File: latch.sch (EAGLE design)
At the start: 32 parts, among them IC1 LM7805, IC2 LM339D, IC3 LM339D, K1 4052, Q1 BS170, Q2 BS170, Q3 BS170, Q4 BS170, Q5 BS170, Q6 BS170, Q7 BS170

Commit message: Second version of latches board
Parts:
- D3: value (none) -> 1N4148
- F1: value 500mA -> 1A
- R10, R5: value 10K -> 2.2K
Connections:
- removed net BMS_RESET_2: IMD_BMS_LATCH-3.S
- new net N$14: Q6.S, Q7.D
- net BMS_STATUS: now also IMD_BMS_LATCH-3.S
- net GND: no longer Q6.S
- net N$13: no longer Q7.D
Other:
- note added: "Drawn by: Luis Suarez"
- note added: "IMD and BMS Latching Board"
- note added: "Reviewed by:"
- note added: "Signal Value Status IMD_FAIL 1 Ok 0 Fail BMS_FAIL 1 Ok 0 Fail"
- note added: "TUC Racing 2016 Formula Student Italy"
- moved on the sheet: D3, K1, Q7

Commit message: Third version of latches board
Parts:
- removed Q1: BS170, transistor-small-signal:BS170
- removed R4: 100K, rcl:R-EU_R1206
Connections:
- removed net IMD_BMS_RESET_1: IMD_BMS_LATCH-4.S, R4.2, RESET_SWITCH.S
- removed net N$4: Q1.G, R4.1
- net DELAY_PWR: now also IMD_BMS_LATCH-4.S, RESET_SWITCH.S; no longer Q1.D
- net GND: no longer Q1.S
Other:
- moved on the sheet: IMD_BMS_LATCH-7, IMD_BMS_LATCH-8, RESET_SWITCH
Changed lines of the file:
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@@
 </layers>
 <schematic xreflabel="%F%N/%S.%C%R" xrefpart="/%S.%C%R">
+<description>IMD and BMS latching board.</description>
 <attributes>
 </attributes>
@@
 <part name="R3" library="rcl" deviceset="R-EU_" device="R1206" value="1K"/>
 <part name="P+5" library="supply1" deviceset="+5V" device=""/>
-<part name="Q1" library="transistor-small-signal" deviceset="BS170" device=""/>
-<part name="GND5" library="supply1" deviceset="GND" device=""/>
-<part name="R4" library="rcl" deviceset="R-EU_" device="R1206" value="100K"/>
 <part name="RESET_SWITCH" library="adafruit" deviceset="SPST" device=""/>
 <part name="GND6" library="supply1" deviceset="GND" device=""/>
@@
 </instance>
 <instance part="F1" gate="G$1" x="40.64" y="154.94"/>
-<instance part="IMD_BMS_LATCH" gate="-7" x="220.98" y="154.94"/>
-<instance part="IMD_BMS_LATCH" gate="-8" x="220.98" y="160.02"/>
+<instance part="IMD_BMS_LATCH" gate="-7" x="220.98" y="160.02"/>
+<instance part="IMD_BMS_LATCH" gate="-8" x="220.98" y="154.94"/>
 <instance part="IMD_BMS_LATCH" gate="-9" x="220.98" y="149.86"/>
 <instance part="IMD_BMS_LATCH" gate="-10" x="220.98" y="144.78"/>
@@
 <attribute name="VALUE" x="53.34" y="106.68" size="1.778" layer="96"/>
 </instance>
-<instance part="Q1" gate="1" x="63.5" y="58.42"/>
-<instance part="GND5" gate="1" x="66.04" y="45.72"/>
-<instance part="R4" gate="G$1" x="50.8" y="58.42" smashed="yes" rot="R180">
-<attribute name="NAME" x="49.53" y="59.9186" size="1.778" layer="95"/>
-<attribute name="VALUE" x="49.53" y="55.118" size="1.778" layer="96"/>
-</instance>
-<instance part="RESET_SWITCH" gate="G$1" x="40.64" y="48.26" smashed="yes">
-<attribute name="NAME" x="34.925" y="48.895" size="1.778" layer="95" rot="R180"/>
-<attribute name="VALUE" x="38.735" y="38.735" size="1.778" layer="96" rot="R90"/>
-</instance>
-<instance part="GND6" gate="1" x="43.18" y="27.94"/>
+<instance part="RESET_SWITCH" gate="G$1" x="60.96" y="60.96" smashed="yes">
+<attribute name="NAME" x="55.245" y="61.595" size="1.778" layer="95" rot="R180"/>
+<attribute name="VALUE" x="59.055" y="51.435" size="1.778" layer="96" rot="R90"/>
+</instance>
+<instance part="GND6" gate="1" x="63.5" y="40.64"/>
 <instance part="R7" gate="G$1" x="119.38" y="106.68" smashed="yes">
 <attribute name="NAME" x="123.19" y="110.871" size="1.778" layer="95" rot="R180"/>
@@
 <pinref part="RESET_SWITCH" gate="G$1" pin="P"/>
 <pinref part="GND6" gate="1" pin="GND"/>
-<wire x1="43.18" y1="43.18" x2="43.18" y2="35.56" width="0.1524" layer="91"/>
-<wire x1="43.18" y1="35.56" x2="43.18" y2="30.48" width="0.1524" layer="91"/>
-<wire x1="43.18" y1="35.56" x2="38.1" y2="35.56" width="0.1524" layer="91"/>
-<label x="38.1" y="35.56" size="1.778" layer="95" rot="R180" xref="yes"/>
-<junction x="43.18" y="35.56"/>
-</segment>
-</net>
-<net name="IMD_BMS_RESET_1" class="0">
-<segment>
-<pinref part="IMD_BMS_LATCH" gate="-4" pin="S"/>
-<wire x1="55.88" y1="142.24" x2="33.02" y2="142.24" width="0.1524" layer="91"/>
-<label x="55.88" y="142.24" size="1.778" layer="95" xref="yes"/>
-</segment>
-<segment>
-<pinref part="R4" gate="G$1" pin="2"/>
-<wire x1="45.72" y1="58.42" x2="43.18" y2="58.42" width="0.1524" layer="91"/>
-<wire x1="43.18" y1="58.42" x2="43.18" y2="55.88" width="0.1524" layer="91"/>
-<pinref part="RESET_SWITCH" gate="G$1" pin="S"/>
-<wire x1="43.18" y1="53.34" x2="43.18" y2="55.88" width="0.1524" layer="91"/>
-<junction x="43.18" y="55.88"/>
-<wire x1="43.18" y1="55.88" x2="38.1" y2="55.88" width="0.1524" layer="91"/>
-<label x="38.1" y="55.88" size="1.778" layer="95" rot="R180" xref="yes"/>
+<wire x1="63.5" y1="55.88" x2="63.5" y2="48.26" width="0.1524" layer="91"/>
+<wire x1="63.5" y1="48.26" x2="63.5" y2="43.18" width="0.1524" layer="91"/>
+<wire x1="63.5" y1="48.26" x2="58.42" y2="48.26" width="0.1524" layer="91"/>
+<label x="58.42" y="48.26" size="1.778" layer="95" rot="R180" xref="yes"/>
+<junction x="63.5" y="48.26"/>
 </segment>
 </net>
@@
 </segment>
 <segment>
-<pinref part="Q1" gate="1" pin="S"/>
-<pinref part="GND5" gate="1" pin="GND"/>
-<wire x1="66.04" y1="53.34" x2="66.04" y2="48.26" width="0.1524" layer="91"/>
-</segment>
-<segment>
 <pinref part="Q2" gate="1" pin="S"/>
 <pinref part="GND7" gate="1" pin="GND"/>
@@
 <segment>
 <pinref part="IMD_BMS_LATCH" gate="-8" pin="S"/>
-<wire x1="218.44" y1="160.02" x2="213.36" y2="160.02" width="0.1524" layer="91"/>
-<label x="213.36" y="160.02" size="1.778" layer="95" rot="R180" xref="yes"/>
+<wire x1="218.44" y1="154.94" x2="213.36" y2="154.94" width="0.1524" layer="91"/>
+<label x="213.36" y="154.94" size="1.778" layer="95" rot="R180" xref="yes"/>
 </segment>
 <segment>
@@
 <segment>
 <pinref part="IMD_BMS_LATCH" gate="-7" pin="S"/>
-<wire x1="218.44" y1="154.94" x2="213.36" y2="154.94" width="0.1524" layer="91"/>
-<label x="213.36" y="154.94" size="1.778" layer="95" rot="R180" xref="yes"/>
+<wire x1="218.44" y1="160.02" x2="213.36" y2="160.02" width="0.1524" layer="91"/>
+<label x="213.36" y="160.02" size="1.778" layer="95" rot="R180" xref="yes"/>
 </segment>
 <segment>
@@
 <wire x1="55.88" y1="91.44" x2="55.88" y2="86.36" width="0.1524" layer="91"/>
 <wire x1="55.88" y1="86.36" x2="50.8" y2="86.36" width="0.1524" layer="91"/>
-<pinref part="Q1" gate="1" pin="D"/>
-<wire x1="55.88" y1="86.36" x2="66.04" y2="86.36" width="0.1524" layer="91"/>
-<wire x1="66.04" y1="86.36" x2="66.04" y2="63.5" width="0.1524" layer="91"/>
-<wire x1="66.04" y1="86.36" x2="71.12" y2="86.36" width="0.1524" layer="91"/>
-<junction x="66.04" y="86.36"/>
+<wire x1="55.88" y1="86.36" x2="63.5" y2="86.36" width="0.1524" layer="91"/>
 <junction x="55.88" y="86.36"/>
 <label x="71.12" y="86.36" size="1.778" layer="95" xref="yes"/>
+<wire x1="63.5" y1="86.36" x2="71.12" y2="86.36" width="0.1524" layer="91"/>
+<wire x1="63.5" y1="86.36" x2="63.5" y2="66.04" width="0.1524" layer="91"/>
+<pinref part="RESET_SWITCH" gate="G$1" pin="S"/>
+<junction x="63.5" y="86.36"/>
 </segment>
 <segment>
@@
 <wire x1="132.08" y1="48.26" x2="132.08" y2="50.8" width="0.1524" layer="91"/>
 <label x="132.08" y="50.8" size="1.778" layer="95" rot="R90" xref="yes"/>
+</segment>
+<segment>
+<pinref part="IMD_BMS_LATCH" gate="-4" pin="S"/>
+<wire x1="55.88" y1="142.24" x2="33.02" y2="142.24" width="0.1524" layer="91"/>
+<label x="55.88" y="142.24" size="1.778" layer="95" xref="yes"/>
 </segment>
 </net>
@@
 </segment>
 </net>
-<net name="N$4" class="0">
-<segment>
-<pinref part="R4" gate="G$1" pin="1"/>
-<pinref part="Q1" gate="1" pin="G"/>
-<wire x1="55.88" y1="58.42" x2="58.42" y2="58.42" width="0.1524" layer="91"/>
-</segment>
-</net>

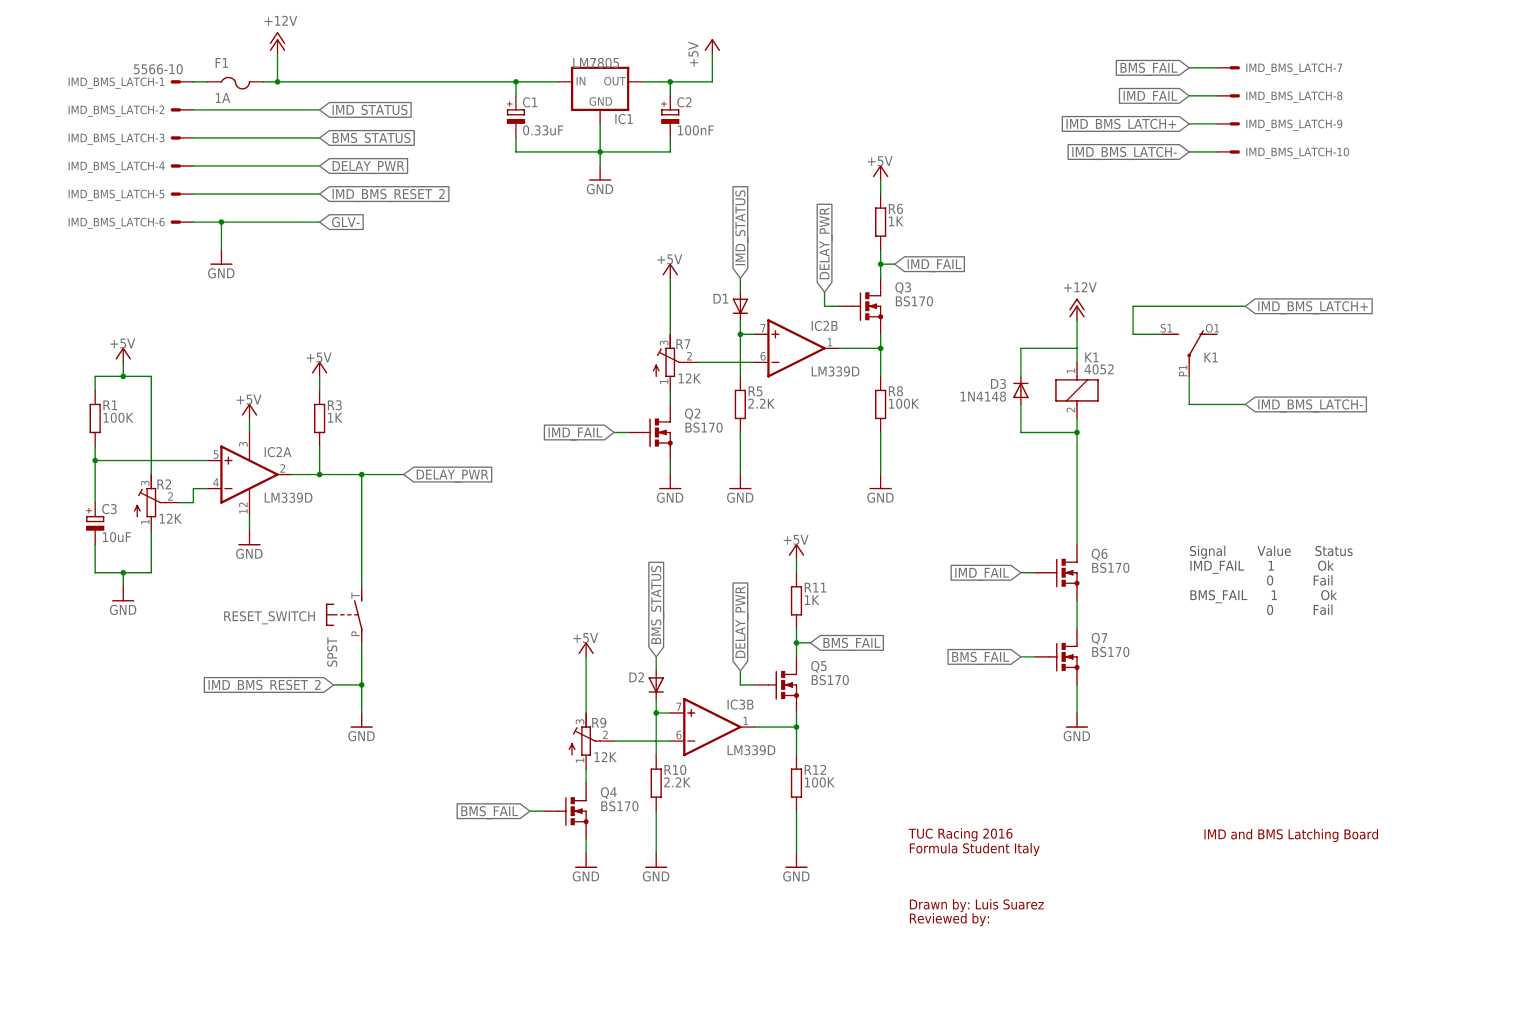
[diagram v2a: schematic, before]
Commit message: Add board design for fourth version
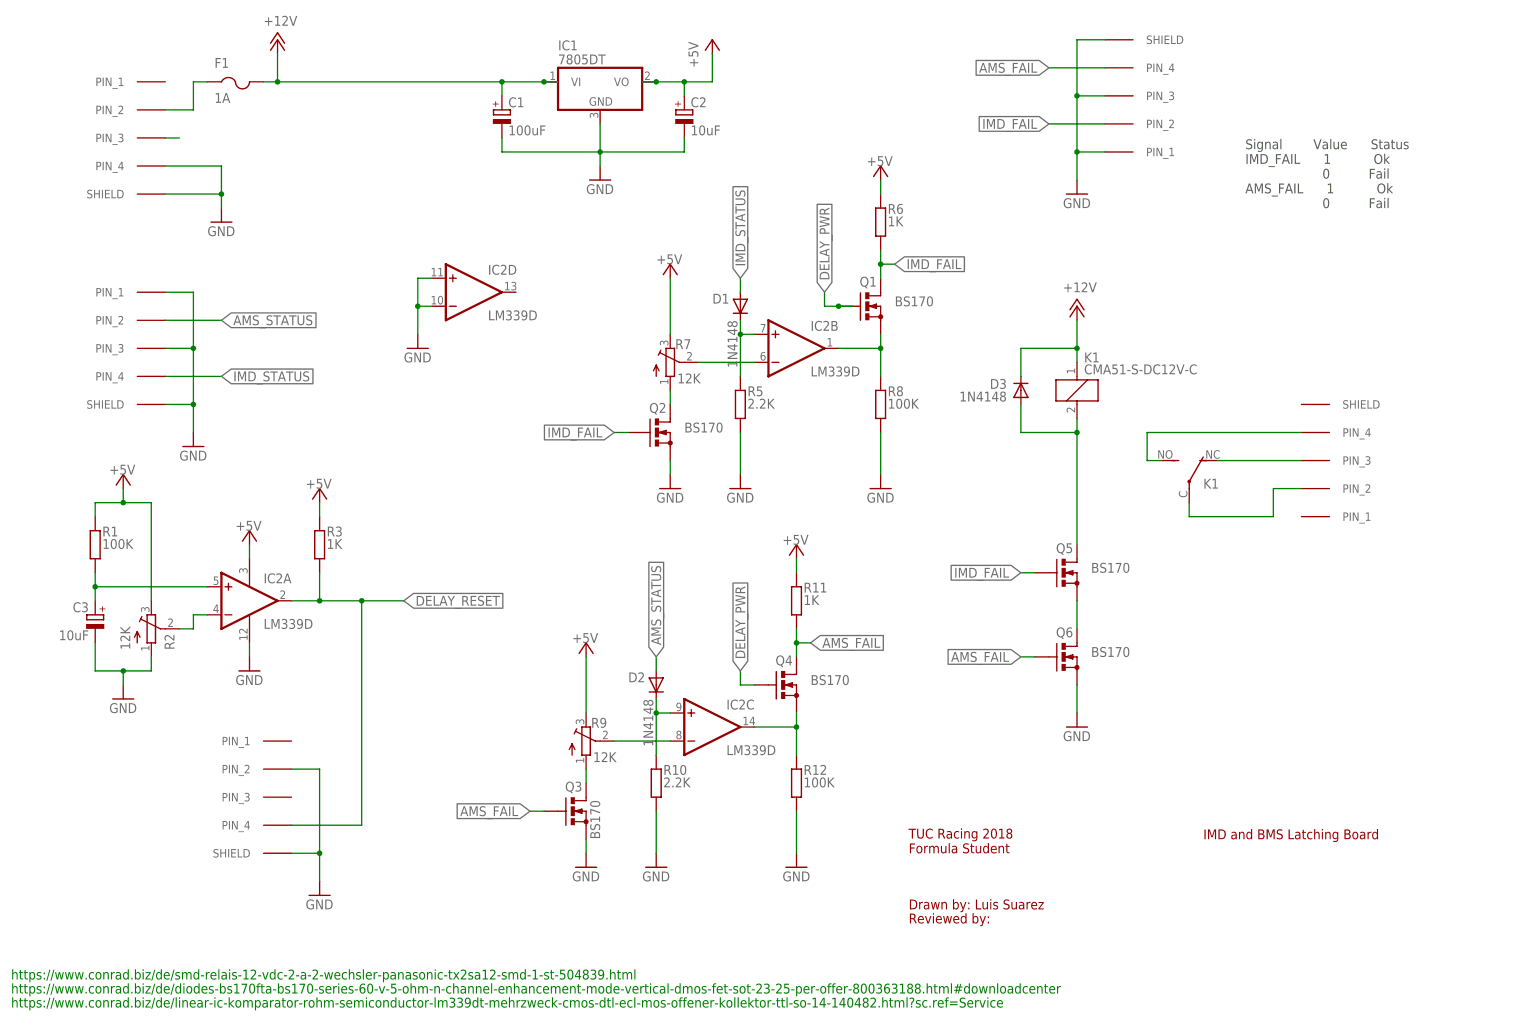
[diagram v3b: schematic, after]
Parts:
- removed IC3: LM339D, linear:LM339D
- removed IMD_BMS_LATCH: 5566-10, con-molex:5566-10
- removed Q7: BS170, transistor-small-signal:BS170
- removed RESET_SWITCH: SPST, adafruit:SPST
- added INDICATORS, RESET: M8-718-FEMALE, SamacSys_Parts:M8-718-FEMALE
- added LATCH, STATUS: M8-718-MALE, SamacSys_Parts:M8-718-MALE
- added POWER_CONN: POWER, SamacSys_Parts:M8-718-MALE
- added Q1: BS170, SamacSys_Parts:BS170FTA
- C1: value 0.33uF -> 100uF; device rcl:CPOL-EU140CLH-1010 -> rcl:CPOL-EUD
- C2: value 100nF -> 10uF; device rcl:CPOL-EU140CLH-1010 -> rcl:CPOL-EUC
- C3: device rcl:CPOL-EU140CLH-0810 -> rcl:CPOL-EUC
- D1, D2: value (none) -> 1N4148; device diode:DIODE-DO-214AC -> diode:DIODE-GF1
- F1: device adafruit:PTCFUSE-1812 -> adafruit:PTCFUSE-1206
- IC1: value LM7805 -> 7805DT; device v-reg:78XX-TO3 -> linear:7805DT
- K1: value 4052 -> CMA51-S-DC12V-C; device relay:4052 -> relay:CQ1-12V
- Q2, Q3, Q4, Q5, Q6: device transistor-small-signal:BS170 -> SamacSys_Parts:BS170FTA
- R1, R10, R11, R12, R3, R5, R6, R8: device rcl:R-EU_R1206 -> rcl:R-EU_R0805
- R2, R7, R9: device rcl:R-TRIMM64Y -> pot:TRIM_EU-SM-42/43B
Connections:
- removed net BMS_FAIL: IMD_BMS_LATCH-7.S, Q4.G, Q5.D, Q7.G, R11.1
- removed net BMS_STATUS: D2.A, IMD_BMS_LATCH-3.S
- removed net GLV-: IMD_BMS_LATCH-6.S
- removed net IMD_BMS_LATCH+: IMD_BMS_LATCH-9.S, K12.S
- removed net IMD_BMS_LATCH-: IMD_BMS_LATCH-10.S, K12.P
- removed net IMD_BMS_RESET_2: IMD_BMS_LATCH-5.S, RESET_SWITCH.P
- removed net N$1: F1.1, IMD_BMS_LATCH-1.S
- new net AMS_FAIL: INDICATORS.PIN_4, Q3.G, Q4.D, Q6.G, R11.1
- new net AMS_STATUS: D2.A, STATUS.PIN_2
- new net DELAY_RESET: IC2A.OUT, R3.1, RESET.PIN_4
- new net LATCH+: K12.S, LATCH.PIN_4
- new net LATCH-: K12.P, LATCH.PIN_2
- new net N$15: POWER_CONN.PIN_3
- new net N$16: K12.O, LATCH.PIN_3
- net +12V: now also C1.+, F1.2, IC1.VI
- net +5V: now also IC1.VO; no longer IC1.OUT
- net DELAY_PWR: now also Q1.G, Q4.G; no longer IC2A.OUT, IMD_BMS_LATCH-4.S, Q3.G, Q5.G, R3.1, RESET_SWITCH.S
- net GLV+: now also F1.1, POWER_CONN.PIN_2; no longer C1.+, F1.2, IC1.IN
- net GND: now also IC2D.+IN, IC2D.-IN, INDICATORS.PIN_1, INDICATORS.PIN_3, INDICATORS.SHIELD, POWER_CONN.PIN_4, POWER_CONN.SHIELD, Q3.S, Q6.S, RESET.PIN_2, RESET.SHIELD, STATUS.PIN_1, STATUS.PIN_3, STATUS.SHIELD; no longer Q4.S, Q7.S
- net IMD_FAIL: now also INDICATORS.PIN_2, Q1.D, Q5.G; no longer IMD_BMS_LATCH-8.S, Q3.D, Q6.G
- net IMD_STATUS: now also STATUS.PIN_4; no longer IMD_BMS_LATCH-2.S
- net N$10: now also IC2C.-IN; no longer IC3B.-IN
- net N$11: now also Q3.D; no longer Q4.D
- net N$12: now also IC2C.OUT, Q4.S; no longer IC3B.OUT, Q5.S
- net N$13: now also Q5.D; no longer Q6.D
- net N$14: now also Q5.S, Q6.D; no longer Q6.S, Q7.D
- net N$8: now also IC2C.+IN; no longer IC3B.+IN
- net N$9: now also Q1.S; no longer Q3.S
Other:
- note added: "Signal Value Status IMD_FAIL 1 Ok 0 Fail AMS_FAIL 1 Ok 0 Fail"
- note added: "TUC Racing 2018 Formula Student"
- note added: "https://www.conrad.biz/de/diodes-bs170fta-bs170-series-60-v-5-ohm-n-channel-enhancement-mode-vertical-dmos-fet-sot-23-25-per-offer-800363188.html#downloadcenter"
- note added: "https://www.conrad.biz/de/linear-ic-komparator-rohm-semiconductor-lm339dt-mehrzweck-cmos-dtl-ecl-mos-offener-kollektor-ttl-so-14-140482.html?sc.ref=Service"
- note added: "https://www.conrad.biz/de/smd-relais-12-vdc-2-a-2-wechsler-panasonic-tx2sa12-smd-1-st-504839.html"
- note removed: "Signal Value Status IMD_FAIL 1 Ok 0 Fail BMS_FAIL 1 Ok 0 Fail"
- note removed: "TUC Racing 2016 Formula Student Italy"
- moved on the sheet: C1, C2, C3, IC2A, K1, R1, R3
